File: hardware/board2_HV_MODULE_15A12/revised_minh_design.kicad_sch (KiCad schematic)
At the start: 19 parts, among them J1 Conn_01x07_Male, J2 Conn_01x01_Male, J3 Conn_01x02_Male, U1 LM7805_TO220, U2 NE5532, U4 15A12

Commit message: cleanup
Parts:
- J2: now left out of the parts list
- R1: value 10k -> 4.7k
- R2: value 4.7k -> 2k
- R4: value 1K -> 2.2k
- R5, R7: value 2K -> 3k9
- R6, R8: value 1.1K -> 1k1
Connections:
- net Earth: now also R3.2; no longer R3.1
- net VPGM: now also R3.1; no longer R3.2
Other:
- note added: "Vout/Vin = 1 + 2/4.7"
- note removed: "Vout/Vin = 1 + 4.7/10"
- moved on the sheet: C1, C2, C3, D1, D2, J1, J2, J3, R1, R2, R3, R4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

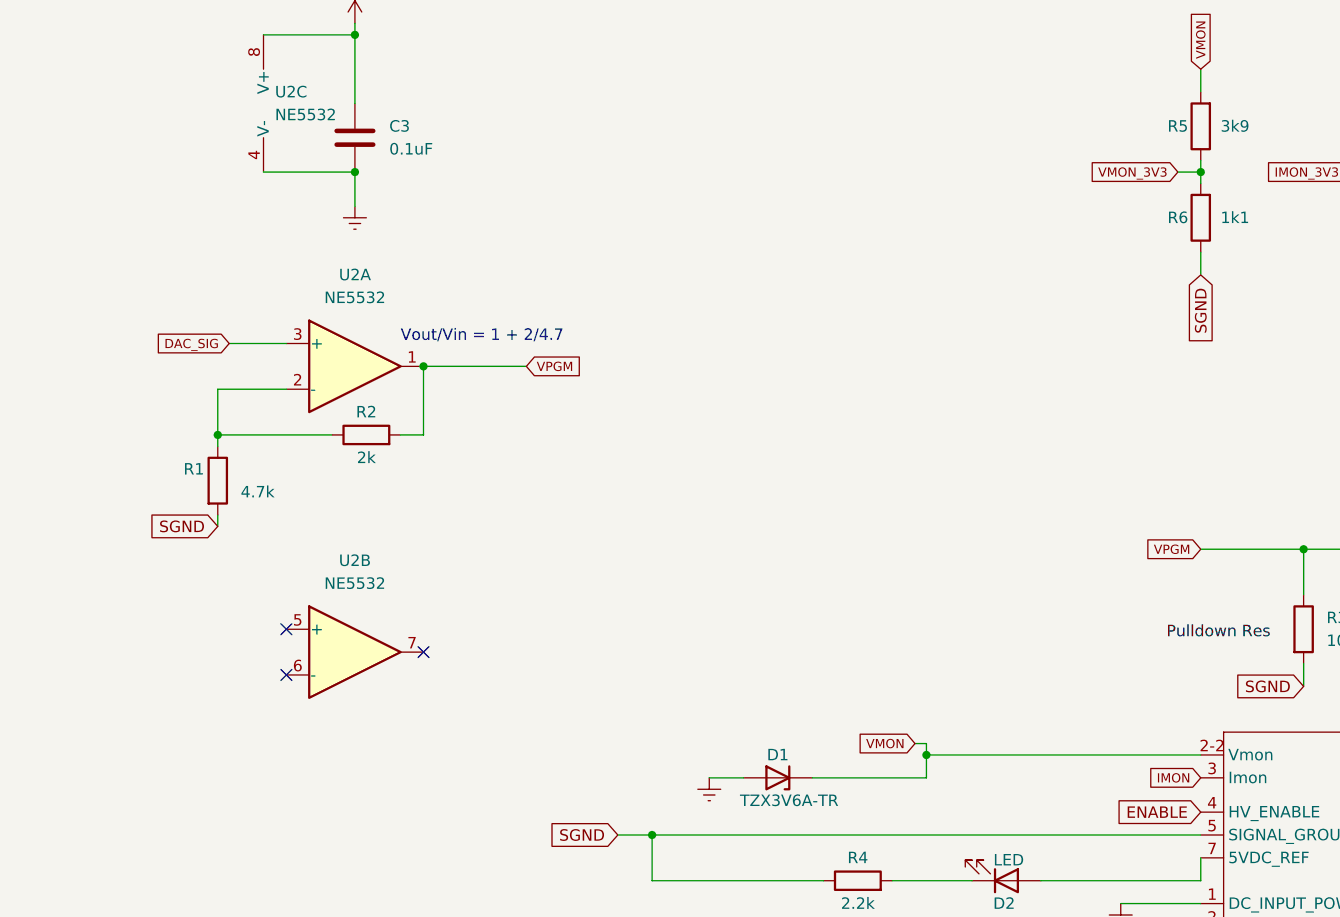
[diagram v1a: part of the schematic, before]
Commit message: Used 2nd opamp for unity gain on VMON
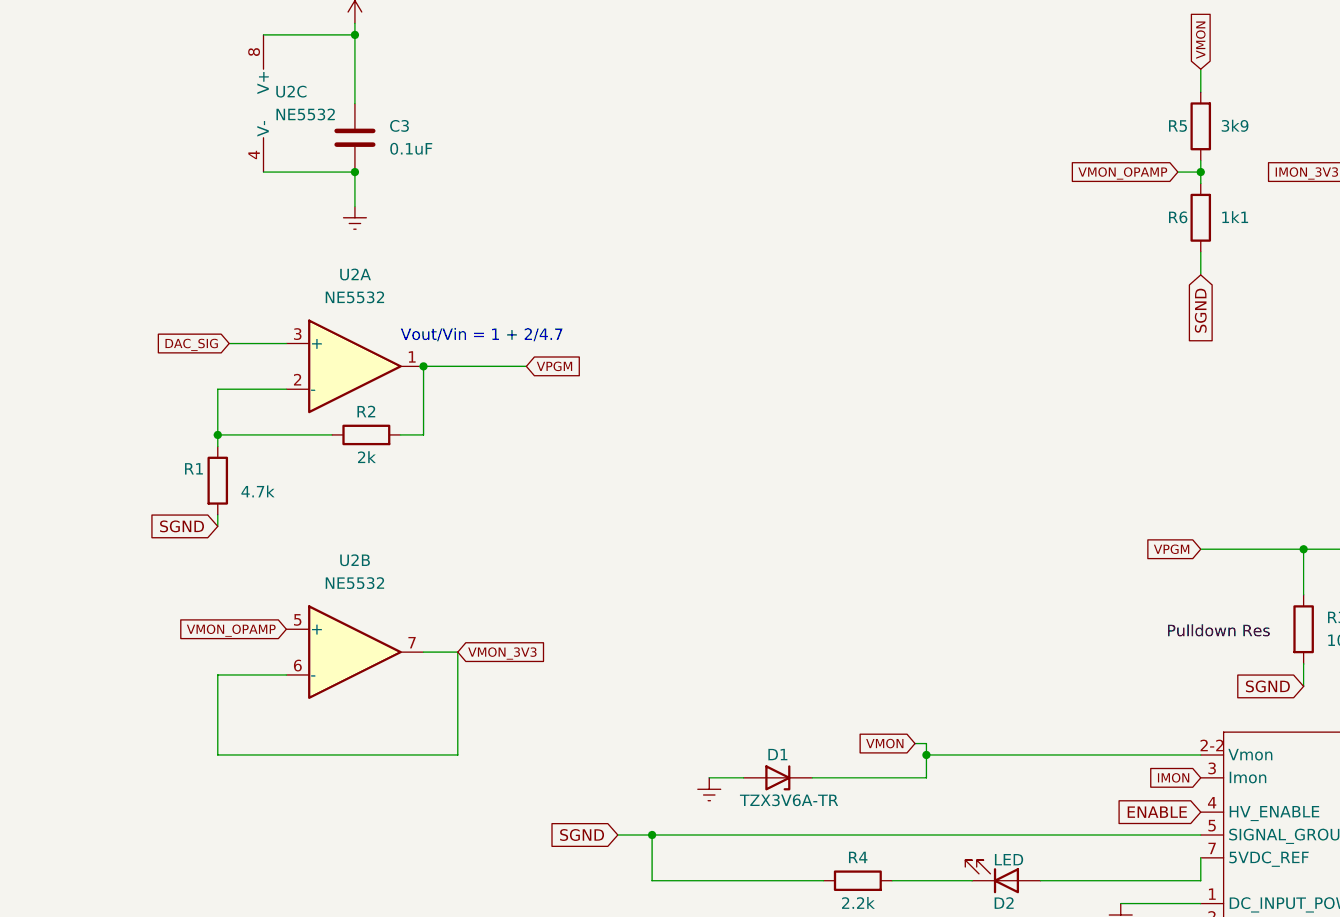
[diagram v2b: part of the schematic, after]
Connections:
- net VMON_3V3: now also U2.6 (-), U2.7; no longer R5.1, R6.2
- net VMON_OPAMP: now reaches U2.5 (+)
- net VMON_OPAMP: now also R5.1, R6.2
- no-connect marks 4 -> 1
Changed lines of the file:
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@@
   )
   (no_connect (at 261.62 144.78))
-  (no_connect (at 132.08 101.6))
-  (no_connect (at 132.08 106.68))
-  (no_connect (at 147.32 104.14))
+  (wire (pts (xy 151.13 104.14) (xy 147.32 104.14))
+    (stroke (width 0) (type default) (color 0 0 0 0))
+  )
   (wire (pts (xy 233.68 49.53) (xy 233.68 50.8))
     (stroke (width 0) (type default) (color 0 0 0 0))
@@
     (stroke (width 0) (type default) (color 0 0 0 0))
   )
+  (wire (pts (xy 151.13 115.57) (xy 124.46 115.57))
+    (stroke (width 0) (type default) (color 0 0 0 0))
+  )
   (wire (pts (xy 38.1 46.99) (xy 53.34 46.99))
     (stroke (width 0) (type default) (color 0 0 0 0))
@@
     (stroke (width 0) (type default) (color 0 0 0 0))
   )
+  (wire (pts (xy 124.46 115.57) (xy 124.46 106.68))
+    (stroke (width 0) (type default) (color 0 0 0 0))
+  )
   (wire (pts (xy 77.47 41.91) (xy 77.47 39.37))
     (stroke (width 0) (type default) (color 0 0 0 0))
@@
     (stroke (width 0) (type default) (color 0 0 0 0))
   )
+  (wire (pts (xy 124.46 106.68) (xy 132.08 106.68))
+    (stroke (width 0) (type default) (color 0 0 0 0))
+  )
   (wire (pts (xy 87.63 34.29) (xy 90.17 34.29))
     (stroke (width 0) (type default) (color 0 0 0 0))
@@
     (stroke (width 0) (type default) (color 0 0 0 0))
   )
+  (wire (pts (xy 151.13 104.14) (xy 151.13 115.57))
+    (stroke (width 0) (type default) (color 0 0 0 0))
+  )
   (wire (pts (xy 252.73 59.69) (xy 252.73 62.23))
     (stroke (width 0) (type default) (color 0 0 0 0))
@@
     )
   )
-  (global_label "VMON_3V3" (shape input) (at 231.14 50.8 180) (fields_autoplaced)
-    (effects (font (size 1.016 1.016)) (justify right))
-    (property "Intersheet References" "${INTERSHEET_REFS}" (id 0) (at 221.4686 50.8635 0)
+  (global_label "VMON_OPAMP" (shape input) (at 231.14 50.8 180) (fields_autoplaced)
+    (effects (font (size 1.016 1.016)) (justify right))
+    (property "Intersheet References" "${INTERSHEET_REFS}" (id 0) (at 219.1464 50.7365 0)
+      (effects (font (size 1.016 1.016)) (justify right) hide)
+    )
+  )
+  (global_label "VMON_OPAMP" (shape input) (at 132.08 101.6 180) (fields_autoplaced)
+    (effects (font (size 1.016 1.016)) (justify right))
+    (property "Intersheet References" "${INTERSHEET_REFS}" (id 0) (at 120.0864 101.5365 0)
       (effects (font (size 1.016 1.016)) (justify right) hide)
     )
@@
       (effects (font (size 1.016 1.016)) (justify left) hide)
     )
+  )
+  (global_label "VMON_3V3" (shape input) (at 151.13 104.14 0) (fields_autoplaced)
+    (effects (font (size 1.016 1.016)) (justify left))
+    (property "Intersheet References" "${INTERSHEET_REFS}" (id 0) (at 160.8014 104.0765 0)
+      (effects (font (size 1.016 1.016)) (justify left) hide)
+    )

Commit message: added BOM Excel
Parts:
- R4: value 2.2k -> 2k
- R5, R7: value 3k9 -> 390k
- R6, R8: value 1k1 -> 110k
- U2: value NE5532 -> LM358
- renumbered U4 to U3
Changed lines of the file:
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@@
     (in_bom yes) (on_board yes)
     (property "Reference" "R6" (id 0) (at 231.14 55.88 0))
-    (property "Value" "1k1" (id 1) (at 237.49 55.88 0))
+    (property "Value" "110k" (id 1) (at 237.49 55.88 0))
     (property "Footprint" "Resistor_THT:R_Axial_DIN0207_L6.3mm_D2.5mm_P10.16mm_Horizontal" (id 2) (at 235.458 55.88 90)
       (effects (font (size 1.27 1.27)) hide)
@@
       (effects (font (size 1.27 1.27)) (justify left))
     )
-    (property "Value" "NE5532" (id 1) (at 130.81 44.4499 0)
+    (property "Value" "LM358" (id 1) (at 130.81 44.4499 0)
       (effects (font (size 1.27 1.27)) (justify left))
     )
@@
       (effects (font (size 1.27 1.27)) hide)
     )
-    (property "Datasheet" "http://www.ti.com/lit/ds/symlink/ne5532.pdf" (id 3) (at 132.08 43.18 0)
+    (property "Datasheet" "https://www.ti.com/lit/ds/symlink/lm358b.pdf?ts=1663950293825&ref_url=https%253A%252F%252Fwww.ti.com%252Fproduct%252FLM358B" (id 3) (at 132.08 43.18 0)
       (effects (font (size 1.27 1.27)) hide)
     )
@@
     (in_bom yes) (on_board yes) (fields_autoplaced)
     (property "Reference" "U2" (id 0) (at 139.7 62.23 0))
-    (property "Value" "NE5532" (id 1) (at 139.7 64.77 0))
+    (property "Value" "LM358" (id 1) (at 139.7 64.77 0))
     (property "Footprint" "Package_DIP:DIP-8_W7.62mm" (id 2) (at 137.16 78.74 0)
       (effects (font (size 1.27 1.27)) hide)
     )
-    (property "Datasheet" "http://www.ti.com/lit/ds/symlink/ne5532.pdf" (id 3) (at 138.43 82.55 0)
+    (property "Datasheet" "https://www.ti.com/lit/ds/symlink/lm358b.pdf?ts=1663950293825&ref_url=https%253A%252F%252Fwww.ti.com%252Fproduct%252FLM358B" (id 3) (at 138.43 82.55 0)
       (effects (font (size 1.27 1.27)) hide)
     )
@@
     (in_bom yes) (on_board yes)
     (property "Reference" "R8" (id 0) (at 250.19 55.88 0))
-    (property "Value" "1k1" (id 1) (at 256.54 55.88 0))
+    (property "Value" "110k" (id 1) (at 256.54 55.88 0))
     (property "Footprint" "Resistor_THT:R_Axial_DIN0207_L6.3mm_D2.5mm_P10.16mm_Horizontal" (id 2) (at 254.508 55.88 90)
       (effects (font (size 1.27 1.27)) hide)
@@
     (in_bom yes) (on_board yes) (fields_autoplaced)
     (property "Reference" "U2" (id 0) (at 139.7 93.98 0))
-    (property "Value" "NE5532" (id 1) (at 139.7 96.52 0))
+    (property "Value" "LM358" (id 1) (at 139.7 96.52 0))
     (property "Footprint" "Package_DIP:DIP-8_W7.62mm" (id 2) (at 139.7 104.14 0)
       (effects (font (size 1.27 1.27)) hide)
     )
-    (property "Datasheet" "http://www.ti.com/lit/ds/symlink/ne5532.pdf" (id 3) (at 139.7 104.14 0)
+    (property "Datasheet" "https://www.ti.com/lit/ds/symlink/lm358b.pdf?ts=1663950293825&ref_url=https%253A%252F%252Fwww.ti.com%252Fproduct%252FLM358B" (id 3) (at 139.7 104.14 0)
       (effects (font (size 1.27 1.27)) hide)
     )
@@
     (in_bom yes) (on_board yes)
     (property "Reference" "R7" (id 0) (at 250.19 45.72 0))
-    (property "Value" "3k9" (id 1) (at 256.54 45.72 0))
+    (property "Value" "390k" (id 1) (at 256.54 45.72 0))
     (property "Footprint" "Resistor_THT:R_Axial_DIN0207_L6.3mm_D2.5mm_P10.16mm_Horizontal" (id 2) (at 254.508 45.72 90)
       (effects (font (size 1.27 1.27)) hide)
@@
     (in_bom yes) (on_board yes)
     (property "Reference" "R5" (id 0) (at 231.14 45.72 0))
-    (property "Value" "3k9" (id 1) (at 237.49 45.72 0))
+    (property "Value" "390k" (id 1) (at 237.49 45.72 0))
     (property "Footprint" "Resistor_THT:R_Axial_DIN0207_L6.3mm_D2.5mm_P10.16mm_Horizontal" (id 2) (at 235.458 45.72 90)
       (effects (font (size 1.27 1.27)) hide)
@@
     (in_bom yes) (on_board yes)
     (property "Reference" "R4" (id 0) (at 195.58 127 90))
-    (property "Value" "2.2k" (id 1) (at 195.58 132.08 90))
+    (property "Value" "2k" (id 1) (at 195.58 132.08 90))
     (property "Footprint" "Resistor_THT:R_Axial_DIN0207_L6.3mm_D2.5mm_P7.62mm_Horizontal" (id 2) (at 195.58 131.318 90)
       (effects (font (size 1.27 1.27)) hide)
@@
   (symbol (lib_id "design:15A12") (at 245.11 121.92 0) (unit 1)
     (in_bom yes) (on_board yes) (fields_autoplaced)
-    (property "Reference" "U4" (id 0) (at 265.43 123.8249 0)
-      (effects (font (size 1.27 1.27)) (justify left))
-    )
-    (property "Value" "15A12" (id 1) (at 265.43 126.3649 0)
+    (property "Reference" "U3" (id 0) (at 265.43 126.3649 0)
+      (effects (font (size 1.27 1.27)) (justify left))
+    )
+    (property "Value" "15A12" (id 1) (at 265.43 128.9049 0)
       (effects (font (size 1.27 1.27)) (justify left))
     )
@@
     )
     (path "/cc15822e-e5c9-440f-88ea-20866b81a034"
-      (reference "R4") (unit 1) (value "2.2k") (footprint "Resistor_THT:R_Axial_DIN0207_L6.3mm_D2.5mm_P7.62mm_Horizontal")
+      (reference "R4") (unit 1) (value "2k") (footprint "Resistor_THT:R_Axial_DIN0207_L6.3mm_D2.5mm_P7.62mm_Horizontal")
     )
     (path "/a4e2fe62-1543-4398-8850-30b5933e3401"
-      (reference "R5") (unit 1) (value "3k9") (footprint "Resistor_THT:R_Axial_DIN0207_L6.3mm_D2.5mm_P10.16mm_Horizontal")
+      (reference "R5") (unit 1) (value "390k") (footprint "Resistor_THT:R_Axial_DIN0207_L6.3mm_D2.5mm_P10.16mm_Horizontal")
     )
     (path "/494f5535-0d2a-461b-8b71-f86f3a6a73ff"
-      (reference "R6") (unit 1) (value "1k1") (footprint "Resistor_THT:R_Axial_DIN0207_L6.3mm_D2.5mm_P10.16mm_Horizontal")
+      (reference "R6") (unit 1) (value "110k") (footprint "Resistor_THT:R_Axial_DIN0207_L6.3mm_D2.5mm_P10.16mm_Horizontal")
     )
     (path "/a2dea781-9bc1-4d50-828e-caa9d3943e1c"
-      (reference "R7") (unit 1) (value "3k9") (footprint "Resistor_THT:R_Axial_DIN0207_L6.3mm_D2.5mm_P10.16mm_Horizontal")
+      (reference "R7") (unit 1) (value "390k") (footprint "Resistor_THT:R_Axial_DIN0207_L6.3mm_D2.5mm_P10.16mm_Horizontal")
     )
     (path "/93d2ccfb-9bbb-4ea8-8868-a325feda37a0"
-      (reference "R8") (unit 1) (value "1k1") (footprint "Resistor_THT:R_Axial_DIN0207_L6.3mm_D2.5mm_P10.16mm_Horizontal")
+      (reference "R8") (unit 1) (value "110k") (footprint "Resistor_THT:R_Axial_DIN0207_L6.3mm_D2.5mm_P10.16mm_Horizontal")
     )
     (path "/34ad081a-2df0-4615-aad1-bf529e317b2a"
@@
     )
     (path "/87c2437d-1195-45fa-a3cc-fd5800dd7242"
-      (reference "U2") (unit 1) (value "NE5532") (footprint "Package_DIP:DIP-8_W7.62mm")
+      (reference "U2") (unit 1) (value "LM358") (footprint "Package_DIP:DIP-8_W7.62mm")
     )
     (path "/9541210e-3eab-414c-a6c0-723cdb681e15"
-      (reference "U2") (unit 2) (value "NE5532") (footprint "Package_DIP:DIP-8_W7.62mm")
+      (reference "U2") (unit 2) (value "LM358") (footprint "Package_DIP:DIP-8_W7.62mm")
     )
     (path "/78cd9dd9-87c1-4d69-87fd-2e37533d7f9d"
-      (reference "U2") (unit 3) (value "NE5532") (footprint "Package_DIP:DIP-8_W7.62mm")
+      (reference "U2") (unit 3) (value "LM358") (footprint "Package_DIP:DIP-8_W7.62mm")
     )
     (path "/e586f466-4d6e-44b1-a629-a3003ee0dde8"
-      (reference "U4") (unit 1) (value "15A12") (footprint "Library:Advanced Energy 15A12P4")
-    )
-  )
+      (reference "U3") (unit 1) (value "15A12") (footprint "Library:Advanced Energy 15A12P4")
+    )
+  )
